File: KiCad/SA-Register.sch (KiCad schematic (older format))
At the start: 60 parts, among them U1 74LVC1G04, U10 74LVC1G32, U11 74LVC1G32, U12 74LVC1G32, U13 74LVC1G32, U14 74LVC1G32, U15 74LVC1G32, U16 74LVC1G32, U17 74LVC1G157, U18 74LVC1G157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

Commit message: PCB v0.2.
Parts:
- D37, D38, D39, D40, D41, D42, D43: value LED_Small -> LED
- U1: value 74LVC1G04 -> SN74LVC1G04DCK
- U10, U11, U12, U13, U14, U15, U16, U3, U5, U6, U7, U8, U9: value 74LVC1G32 -> SN74LVC1G32DCK
- U17, U18, U19, U20, U21, U22, U23: value 74LVC1G157 -> 74LVC1G157GW
- U2: value 74LVC1G08 -> SN74LVC1G08DCK
- U24: value 74LS377 -> SN74HC377DW
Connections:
- net Q0 is gone; now on net OUT_1: R61.2
- net OUT_1: no longer R62.2
- net OUT_2: now also R62.2; no longer R63.2
- net OUT_3: now also R63.2; no longer R64.2
- net OUT_4: now also R64.2; no longer R65.2
- net OUT_5: now also R65.2; no longer R66.2
- net OUT_6: now also R66.2; no longer R67.2
- net OUT_7: now also R67.2
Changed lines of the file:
@@
 P 6700 1550
 F 0 "U5" H 6850 1450 50  0000 C CNN
-F 1 "74LVC1G32" H 6400 1750 50  0000 C CNN
+F 1 "SN74LVC1G32DCK" H 6300 1750 50  0000 C CNN
 F 2 "Package_TO_SOT_SMD:SOT-353_SC-70-5" H 6700 1550 50  0001 C CNN
 F 3 "http://www.ti.com/lit/sg/scyt129e/scyt129e.pdf" H 6700 1550 50  0001 C CNN
@@
 P 6700 2450
 F 0 "U6" H 6850 2350 50  0000 C CNN
-F 1 "74LVC1G32" H 6400 2650 50  0000 C CNN
+F 1 "SN74LVC1G32DCK" H 6300 2650 50  0000 C CNN
 F 2 "Package_TO_SOT_SMD:SOT-353_SC-70-5" H 6700 2450 50  0001 C CNN
 F 3 "http://www.ti.com/lit/sg/scyt129e/scyt129e.pdf" H 6700 2450 50  0001 C CNN
@@
 P 6700 5100
 F 0 "U9" H 6850 5000 50  0000 C CNN
-F 1 "74LVC1G32" H 6400 5300 50  0000 C CNN
+F 1 "SN74LVC1G32DCK" H 6300 5300 50  0000 C CNN
 F 2 "Package_TO_SOT_SMD:SOT-353_SC-70-5" H 6700 5100 50  0001 C CNN
 F 3 "http://www.ti.com/lit/sg/scyt129e/scyt129e.pdf" H 6700 5100 50  0001 C CNN
@@
 P 6700 6000
 F 0 "U10" H 6850 5900 50  0000 C CNN
-F 1 "74LVC1G32" H 6400 6200 50  0000 C CNN
+F 1 "SN74LVC1G32DCK" H 6250 6200 50  0000 C CNN
 F 2 "Package_TO_SOT_SMD:SOT-353_SC-70-5" H 6700 6000 50  0001 C CNN
 F 3 "http://www.ti.com/lit/sg/scyt129e/scyt129e.pdf" H 6700 6000 50  0001 C CNN
@@
 P 6700 6900
 F 0 "U11" H 6850 6800 50  0000 C CNN
-F 1 "74LVC1G32" H 6400 7100 50  0000 C CNN
+F 1 "SN74LVC1G32DCK" H 6250 7100 50  0000 C CNN
 F 2 "Package_TO_SOT_SMD:SOT-353_SC-70-5" H 6700 6900 50  0001 C CNN
 F 3 "http://www.ti.com/lit/sg/scyt129e/scyt129e.pdf" H 6700 6900 50  0001 C CNN
@@
 P 6700 4250
 F 0 "U8" H 6850 4150 50  0000 C CNN
-F 1 "74LVC1G32" H 6400 4450 50  0000 C CNN
+F 1 "SN74LVC1G32DCK" H 6300 4450 50  0000 C CNN
 F 2 "Package_TO_SOT_SMD:SOT-353_SC-70-5" H 6700 4250 50  0001 C CNN
 F 3 "http://www.ti.com/lit/sg/scyt129e/scyt129e.pdf" H 6700 4250 50  0001 C CNN
@@
 P 6700 3350
 F 0 "U7" H 6850 3250 50  0000 C CNN
-F 1 "74LVC1G32" H 6400 3550 50  0000 C CNN
+F 1 "SN74LVC1G32DCK" H 6300 3550 50  0000 C CNN
 F 2 "Package_TO_SOT_SMD:SOT-353_SC-70-5" H 6700 3350 50  0001 C CNN
 F 3 "http://www.ti.com/lit/sg/scyt129e/scyt129e.pdf" H 6700 3350 50  0001 C CNN
@@
 Text HLabel 7050 6000 2    50   Output ~ 0
 DAC_2
-Text Label 1000 10450 0    50   ~ 0
+Text Label 1000 10350 0    50   ~ 0
 Q6
-Text Label 1000 10350 0    50   ~ 0
+Text Label 1000 10250 0    50   ~ 0
 Q5
-Text Label 1000 10250 0    50   ~ 0
+Text Label 1000 10150 0    50   ~ 0
 Q4
-Text Label 1000 10150 0    50   ~ 0
+Text Label 1000 10050 0    50   ~ 0
 Q3
-Text Label 1000 10050 0    50   ~ 0
+Text Label 1000 9950 0    50   ~ 0
 Q2
-Text Label 1000 9950 0    50   ~ 0
+Text Label 1000 9850 0    50   ~ 0
 Q1
-Text Label 1000 9850 0    50   ~ 0
-Q0
 $Comp
 L Device:R_Small R?
@@
 AR Path="/5E362800/5E3E9AD8" Ref="D37"  Part="1"
 F 0 "D37" H 2000 9800 50  0000 C CNN
-F 1 "LED_Small" H 1650 9800 50  0000 C CNN
+F 1 "LED" H 1650 9800 50  0000 C CNN
 F 2 "LED_SMD:LED_0603_1608Metric" V 1900 9850 50  0001 C CNN
 F 3 "~" V 1900 9850 50  0001 C CNN
@@
 AR Path="/5E362800/5E3E9B19" Ref="D43"  Part="1"
 F 0 "D43" H 2000 10400 50  0000 C CNN
-F 1 "LED_Small" H 1650 10400 50  0000 C CNN
+F 1 "LED" H 1650 10400 50  0000 C CNN
 F 2 "LED_SMD:LED_0603_1608Metric" V 1900 10450 50  0001 C CNN
 F 3 "~" V 1900 10450 50  0001 C CNN
@@
 AR Path="/5E362800/5E3E9B21" Ref="D42"  Part="1"
 F 0 "D42" H 2000 10300 50  0000 C CNN
-F 1 "LED_Small" H 1650 10300 50  0000 C CNN
+F 1 "LED" H 1650 10300 50  0000 C CNN
 F 2 "LED_SMD:LED_0603_1608Metric" V 1900 10350 50  0001 C CNN
 F 3 "~" V 1900 10350 50  0001 C CNN
@@
 AR Path="/5E362800/5E3E9B27" Ref="D41"  Part="1"
 F 0 "D41" H 2000 10200 50  0000 C CNN
-F 1 "LED_Small" H 1650 10200 50  0000 C CNN
+F 1 "LED" H 1650 10200 50  0000 C CNN
 F 2 "LED_SMD:LED_0603_1608Metric" V 1900 10250 50  0001 C CNN
 F 3 "~" V 1900 10250 50  0001 C CNN
@@
 AR Path="/5E362800/5E3E9B2F" Ref="D40"  Part="1"
 F 0 "D40" H 2000 10100 50  0000 C CNN
-F 1 "LED_Small" H 1650 10100 50  0000 C CNN
+F 1 "LED" H 1650 10100 50  0000 C CNN
 F 2 "LED_SMD:LED_0603_1608Metric" V 1900 10150 50  0001 C CNN
 F 3 "~" V 1900 10150 50  0001 C CNN
@@
 AR Path="/5E362800/5E3E9B35" Ref="D39"  Part="1"
 F 0 "D39" H 2000 10000 50  0000 C CNN
-F 1 "LED_Small" H 1650 10000 50  0000 C CNN
+F 1 "LED" H 1650 10000 50  0000 C CNN
 F 2 "LED_SMD:LED_0603_1608Metric" V 1900 10050 50  0001 C CNN
 F 3 "~" V 1900 10050 50  0001 C CNN
@@
 AR Path="/5E362800/5E3E9B3C" Ref="D38"  Part="1"
 F 0 "D38" H 2000 9900 50  0000 C CNN
-F 1 "LED_Small" H 1650 9900 50  0000 C CNN
+F 1 "LED" H 1650 9900 50  0000 C CNN
 F 2 "LED_SMD:LED_0603_1608Metric" V 1900 9950 50  0001 C CNN
 F 3 "~" V 1900 9950 50  0001 C CNN
@@
 Wire Wire Line
 	1350 10350 1000 10350
-Wire Wire Line
-	1350 10450 1000 10450
 Wire Wire Line
 	2400 9850 2400 9950
@@
 P 5800 8500
 F 0 "U24" H 5900 9250 50  0000 C CNN
-F 1 "74LS377" H 6000 9150 50  0000 C CNN
+F 1 "SN74HC377DW" H 6150 9150 50  0000 C CNN
 F 2 "Package_SO:SOIC-20W_7.5x12.8mm_P1.27mm" H 5800 8500 50  0001 C CNN
 F 3 "http://www.ti.com/lit/gpn/sn74LS377" H 5800 8500 50  0001 C CNN
@@
 P 4250 1150
 F 0 "U17" H 4544 1196 50  0000 L CNN
-F 1 "74LVC1G157" H 4000 600 50  0000 L CNN
+F 1 "74LVC1G157GW" H 4000 600 50  0000 L CNN
 F 2 "Package_TO_SOT_SMD:SOT-363_SC-70-6" H 3950 575 50  0001 C CNN
 F 3 "" H 3950 575 50  0001 C CNN
@@
 P 4250 3650
 F 0 "U19" H 4544 3696 50  0000 L CNN
-F 1 "74LVC1G157" H 4000 3100 50  0000 L CNN
+F 1 "74LVC1G157GW" H 4000 3100 50  0000 L CNN
 F 2 "Package_TO_SOT_SMD:SOT-363_SC-70-6" H 3950 3075 50  0001 C CNN
 F 3 "" H 3950 3075 50  0001 C CNN
@@
 P 4250 4900
 F 0 "U20" H 4544 4946 50  0000 L CNN
-F 1 "74LVC1G157" H 4000 4350 50  0000 L CNN
+F 1 "74LVC1G157GW" H 4000 4350 50  0000 L CNN
 F 2 "Package_TO_SOT_SMD:SOT-363_SC-70-6" H 3950 4325 50  0001 C CNN
 F 3 "" H 3950 4325 50  0001 C CNN
@@
 P 4250 6100
 F 0 "U21" H 4544 6146 50  0000 L CNN
-F 1 "74LVC1G157" H 4000 5550 50  0000 L CNN
+F 1 "74LVC1G157GW" H 4000 5550 50  0000 L CNN
 F 2 "Package_TO_SOT_SMD:SOT-363_SC-70-6" H 3950 5525 50  0001 C CNN
 F 3 "" H 3950 5525 50  0001 C CNN
@@
 P 4250 7350
 F 0 "U22" H 4544 7396 50  0000 L CNN
-F 1 "74LVC1G157" H 4000 6800 50  0000 L CNN
+F 1 "74LVC1G157GW" H 4000 6800 50  0000 L CNN
 F 2 "Package_TO_SOT_SMD:SOT-363_SC-70-6" H 3950 6775 50  0001 C CNN
 F 3 "" H 3950 6775 50  0001 C CNN
@@
 P 4250 8600
 F 0 "U23" H 4544 8646 50  0000 L CNN
-F 1 "74LVC1G157" H 4000 8050 50  0000 L CNN
+F 1 "74LVC1G157GW" H 4000 8050 50  0000 L CNN
 F 2 "Package_TO_SOT_SMD:SOT-363_SC-70-6" H 3950 8025 50  0001 C CNN
 F 3 "" H 3950 8025 50  0001 C CNN
@@
 P 3350 2750
 F 0 "U3" H 3500 2650 50  0000 C CNN
-F 1 "74LVC1G32" H 3050 2950 50  0000 C CNN
+F 1 "SN74LVC1G32DCK" H 2950 2950 50  0000 C CNN
 F 2 "Package_TO_SOT_SMD:SOT-353_SC-70-5" H 3350 2750 50  0001 C CNN
 F 3 "http://www.ti.com/lit/sg/scyt129e/scyt129e.pdf" H 3350 2750 50  0001 C CNN
@@
 AR Path="/5E362800/5F72A894" Ref="U1"  Part="1"
 F 0 "U1" H 1850 1250 50  0000 C CNN
-F 1 "74LVC1G04" H 1700 650 50  0000 C CNN
+F 1 "SN74LVC1G04DCK" H 1700 650 50  0000 C CNN
 F 2 "Package_TO_SOT_SMD:SOT-353_SC-70-5" H 1700 1050 50  0001 C CNN
 F 3 "http://www.ti.com/lit/sg/scyt129e/scyt129e.pdf" H 1700 1050 50  0001 C CNN
@@
 P 3350 4000
 F 0 "U12" H 3500 3900 50  0000 C CNN
-F 1 "74LVC1G32" H 3050 4200 50  0000 C CNN
+F 1 "SN74LVC1G32DCK" H 2950 4200 50  0000 C CNN
 F 2 "Package_TO_SOT_SMD:SOT-353_SC-70-5" H 3350 4000 50  0001 C CNN
 F 3 "http://www.ti.com/lit/sg/scyt129e/scyt129e.pdf" H 3350 4000 50  0001 C CNN
@@
 P 3350 5250
 F 0 "U13" H 3500 5150 50  0000 C CNN
-F 1 "74LVC1G32" H 3050 5450 50  0000 C CNN
+F 1 "SN74LVC1G32DCK" H 2950 5450 50  0000 C CNN
 F 2 "Package_TO_SOT_SMD:SOT-353_SC-70-5" H 3350 5250 50  0001 C CNN
 F 3 "http://www.ti.com/lit/sg/scyt129e/scyt129e.pdf" H 3350 5250 50  0001 C CNN
@@
 P 3350 6450
 F 0 "U14" H 3500 6350 50  0000 C CNN
-F 1 "74LVC1G32" H 3050 6650 50  0000 C CNN
+F 1 "SN74LVC1G32DCK" H 2950 6650 50  0000 C CNN
 F 2 "Package_TO_SOT_SMD:SOT-353_SC-70-5" H 3350 6450 50  0001 C CNN
 F 3 "http://www.ti.com/lit/sg/scyt129e/scyt129e.pdf" H 3350 6450 50  0001 C CNN
@@
 P 3350 7700
 F 0 "U15" H 3500 7600 50  0000 C CNN
-F 1 "74LVC1G32" H 3050 7900 50  0000 C CNN
+F 1 "SN74LVC1G32DCK" H 2950 7900 50  0000 C CNN
 F 2 "Package_TO_SOT_SMD:SOT-353_SC-70-5" H 3350 7700 50  0001 C CNN
 F 3 "http://www.ti.com/lit/sg/scyt129e/scyt129e.pdf" H 3350 7700 50  0001 C CNN
@@
 P 3350 8950
 F 0 "U16" H 3500 8850 50  0000 C CNN
-F 1 "74LVC1G32" H 3050 9150 50  0000 C CNN
+F 1 "SN74LVC1G32DCK" H 2950 9150 50  0000 C CNN
 F 2 "Package_TO_SOT_SMD:SOT-353_SC-70-5" H 3350 8950 50  0001 C CNN
 F 3 "http://www.ti.com/lit/sg/scyt129e/scyt129e.pdf" H 3350 8950 50  0001 C CNN
@@
 P 2500 1100
 F 0 "U2" H 2350 700 50  0000 C CNN
-F 1 "74LVC1G08" H 2500 800 50  0000 C CNN
+F 1 "SN74LVC1G08DCK" H 2500 800 50  0000 C CNN
 F 2 "Package_TO_SOT_SMD:SOT-353_SC-70-5" H 2500 1100 50  0001 C CNN
 F 3 "http://www.ti.com/lit/sg/scyt129e/scyt129e.pdf" H 2500 1100 50  0001 C CNN
@@
 P 4250 2400
 F 0 "U18" H 4544 2446 50  0000 L CNN
-F 1 "74LVC1G157" H 4000 1850 50  0000 L CNN
+F 1 "74LVC1G157GW" H 4000 1850 50  0000 L CNN
 F 2 "Package_TO_SOT_SMD:SOT-363_SC-70-6" H 3950 1825 50  0001 C CNN
 F 3 "" H 3950 1825 50  0001 C CNN
@@
 Wire Wire Line
 	6400 6850 6150 6850
+Wire Wire Line
+	1350 10450 1000 10450
+Text Label 1000 10450 0    50   ~ 0
+Q7
 $EndSCHEMATC

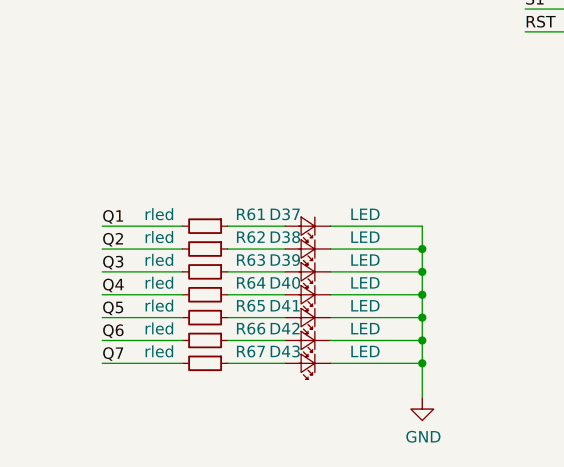
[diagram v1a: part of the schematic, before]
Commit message: v0.3 Changed to Schmitt-Trigger ICs Added pull-down resistor to Clock Enable
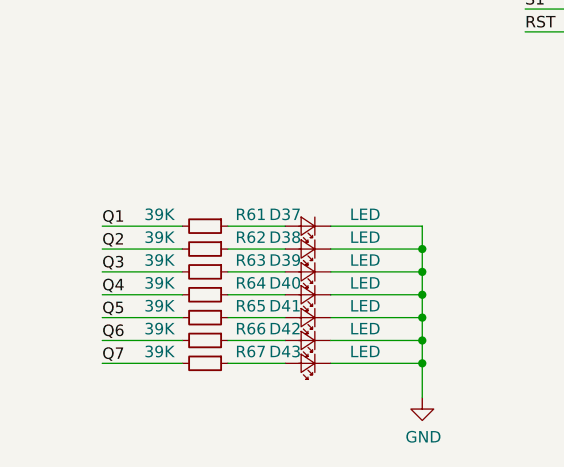
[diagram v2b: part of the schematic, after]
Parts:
- R61, R62, R63, R64, R65, R66, R67: value rled -> 39K
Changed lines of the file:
@@
 Sheet 9 9
 Title "Schilk_SA-ADC"
-Date "2020-02-03"
-Rev "v0.0 (Prod.)"
+Date "2020-08-26"
+Rev "v0.3"
 Comp ""
 Comment1 ""
@@
 AR Path="/5E362800/5E3E9AD2" Ref="R61"  Part="1"
 F 0 "R61" V 1400 10050 50  0000 C CNN
-F 1 "rled" V 1400 9650 50  0000 C CNN
+F 1 "39K" V 1400 9650 50  0000 C CNN
 F 2 "Resistor_SMD:R_0603_1608Metric" H 1450 9850 50  0001 C CNN
 F 3 "~" H 1450 9850 50  0001 C CNN
@@
 AR Path="/5E362800/5E3E9ADF" Ref="R62"  Part="1"
 F 0 "R62" V 1400 10150 50  0000 C CNN
-F 1 "rled" V 1400 9750 50  0000 C CNN
+F 1 "39K" V 1400 9750 50  0000 C CNN
 F 2 "Resistor_SMD:R_0603_1608Metric" H 1450 9950 50  0001 C CNN
 F 3 "~" H 1450 9950 50  0001 C CNN
@@
 AR Path="/5E362800/5E3E9AE7" Ref="R63"  Part="1"
 F 0 "R63" V 1400 10250 50  0000 C CNN
-F 1 "rled" V 1400 9850 50  0000 C CNN
+F 1 "39K" V 1400 9850 50  0000 C CNN
 F 2 "Resistor_SMD:R_0603_1608Metric" H 1450 10050 50  0001 C CNN
 F 3 "~" H 1450 10050 50  0001 C CNN
@@
 AR Path="/5E362800/5E3E9AEE" Ref="R64"  Part="1"
 F 0 "R64" V 1400 10350 50  0000 C CNN
-F 1 "rled" V 1400 9950 50  0000 C CNN
+F 1 "39K" V 1400 9950 50  0000 C CNN
 F 2 "Resistor_SMD:R_0603_1608Metric" H 1450 10150 50  0001 C CNN
 F 3 "~" H 1450 10150 50  0001 C CNN
@@
 AR Path="/5E362800/5E3E9AF5" Ref="R65"  Part="1"
 F 0 "R65" V 1400 10450 50  0000 C CNN
-F 1 "rled" V 1400 10050 50  0000 C CNN
+F 1 "39K" V 1400 10050 50  0000 C CNN
 F 2 "Resistor_SMD:R_0603_1608Metric" H 1450 10250 50  0001 C CNN
 F 3 "~" H 1450 10250 50  0001 C CNN
@@
 AR Path="/5E362800/5E3E9AFC" Ref="R66"  Part="1"
 F 0 "R66" V 1400 10550 50  0000 C CNN
-F 1 "rled" V 1400 10150 50  0000 C CNN
+F 1 "39K" V 1400 10150 50  0000 C CNN
 F 2 "Resistor_SMD:R_0603_1608Metric" H 1450 10350 50  0001 C CNN
 F 3 "~" H 1450 10350 50  0001 C CNN
@@
 AR Path="/5E362800/5E3E9B03" Ref="R67"  Part="1"
 F 0 "R67" V 1400 10650 50  0000 C CNN
-F 1 "rled" V 1400 10250 50  0000 C CNN
+F 1 "39K" V 1400 10250 50  0000 C CNN
 F 2 "Resistor_SMD:R_0603_1608Metric" H 1450 10450 50  0001 C CNN
 F 3 "~" H 1450 10450 50  0001 C CNN
